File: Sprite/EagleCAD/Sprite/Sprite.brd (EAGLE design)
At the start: 35 x 35 mm, 22 parts, among them Q1 26MHz, U1 CC430F5137, U2 HMC5883LSMD, U3 ITG-3200

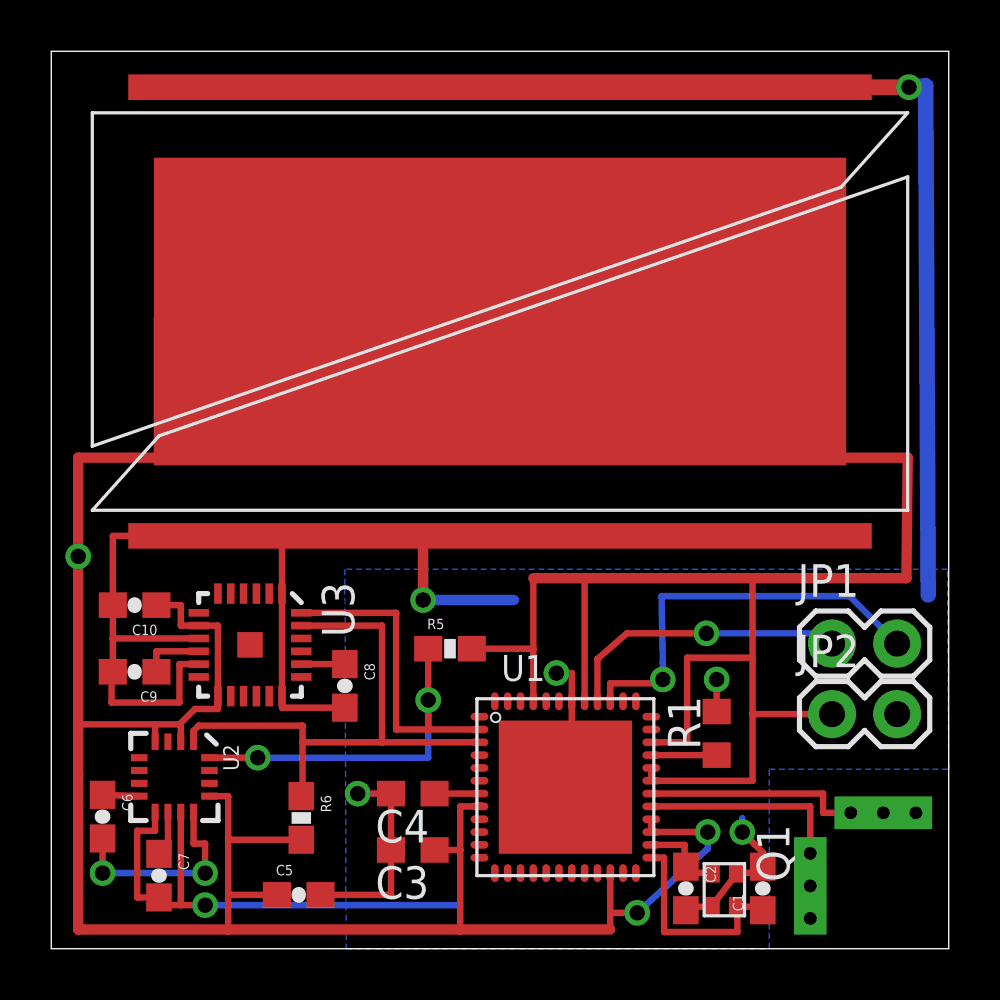
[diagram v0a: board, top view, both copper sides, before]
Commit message: Revert "Moved GND strip closer to TASC cells + removed bottom cells"
This reverts commit a51b0ba4fb3e3dccbe7975012f3db8ac667cb900.
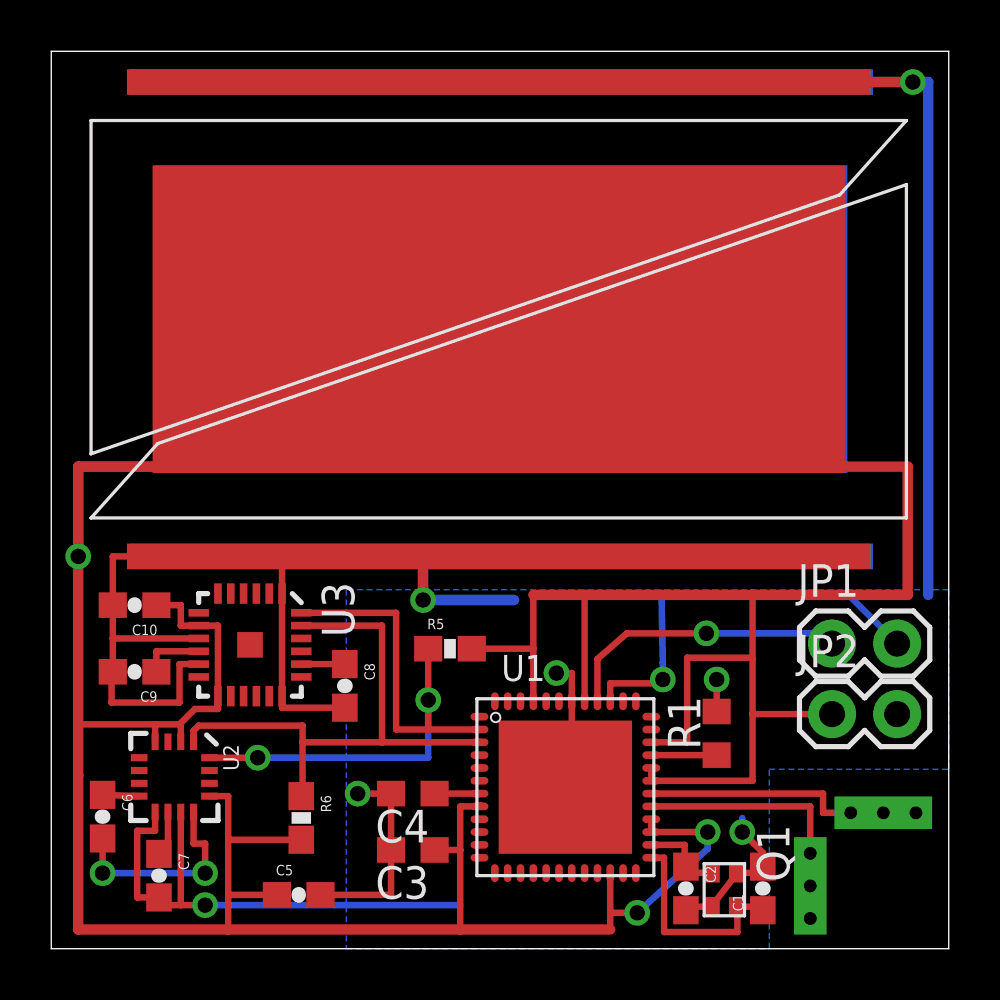
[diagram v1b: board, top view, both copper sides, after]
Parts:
- added S2: TASC, TASC:TASC
- moved S1 0.30 mm to (1.55, 16.8)
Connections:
- net GND: now also S2.MINUS1, S2.MINUS2
- net VCC: now also S2.PLUS
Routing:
- net VCC: track 158.8 -> 182.9 mm
- net GND: track 131.1 -> 137.9 mm
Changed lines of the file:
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@@
 </autorouter>
 <elements>
-<element name="S1" library="TASC" package="TASC" value="TASC" x="1.6" y="17.1"/>
+<element name="S1" library="TASC" package="TASC" value="TASC" x="1.55" y="16.8"/>
+<element name="S2" library="TASC" package="TASC" value="TASC" x="33.45" y="16.8" rot="MR0"/>
 <element name="U1" library="TI_MSP430_v16" package="RGZ48" value="CC430F5137" x="20.05" y="6.3"/>
 <element name="Q1" library="ABM11_JAA" package="ABM11_CERAMIC-SMD-CRYSTAL" value="26MHz" x="26.25" y="2.3" rot="R270"/>
@@
 <signal name="VCC">
 <contactref element="S1" pad="PLUS"/>
+<contactref element="S2" pad="PLUS"/>
 <contactref element="U1" pad="27"/>
 <contactref element="U1" pad="22"/>
@@
 <contactref element="R5" pad="2"/>
 <contactref element="R6" pad="2"/>
-<wire x1="17.5" y1="24.85" x2="4.2" y2="24.55" width="0.4064" layer="1"/>
-<wire x1="4.2" y1="24.55" x2="4.2" y2="19.15" width="0.4064" layer="1"/>
-<wire x1="4.2" y1="19.15" x2="1.05" y2="19.15" width="0.4064" layer="1"/>
-<wire x1="1.05" y1="19.15" x2="1.05" y2="15.3" width="0.4064" layer="1"/>
+<wire x1="17.45" y1="24.55" x2="4.2" y2="24.55" width="0.4064" layer="1"/>
+<wire x1="4.2" y1="24.55" x2="4.2" y2="18.8" width="0.4064" layer="1"/>
+<wire x1="4.2" y1="18.8" x2="1.05" y2="18.8" width="0.4064" layer="1"/>
+<wire x1="1.05" y1="18.8" x2="1.05" y2="15.3" width="0.4064" layer="1"/>
+<wire x1="17.55" y1="24.55" x2="4.2" y2="24.55" width="0.4064" layer="16"/>
+<wire x1="4.2" y1="24.55" x2="4.2" y2="18.8" width="0.4064" layer="16"/>
+<wire x1="4.2" y1="18.8" x2="1.05" y2="18.8" width="0.4064" layer="16"/>
+<wire x1="1.05" y1="18.8" x2="1.05" y2="15.3" width="0.4064" layer="16"/>
 <via x="1.05" y="15.3" extent="1-16" drill="0.6"/>
 <wire x1="16.7" y1="5.55" x2="16.75" y2="5.6" width="0.254" layer="1"/>
-<wire x1="33.35" y1="14.45" x2="33.4" y2="19.15" width="0.4064" layer="1"/>
-<wire x1="33.4" y1="19.15" x2="30.7" y2="19.15" width="0.4064" layer="1"/>
+<wire x1="33.4" y1="13.8" x2="33.4" y2="18.8" width="0.4064" layer="1"/>
+<wire x1="33.4" y1="18.8" x2="30.7" y2="18.8" width="0.4064" layer="1"/>
 <wire x1="16.7" y1="5.55" x2="15.95" y2="5.55" width="0.254" layer="1"/>
 <wire x1="15.95" y1="3.85" x2="14.95" y2="3.85" width="0.254" layer="1"/>
-<wire x1="33.35" y1="14.45" x2="27.35" y2="14.45" width="0.4064" layer="1"/>
-<wire x1="27.35" y1="14.45" x2="20.8" y2="14.45" width="0.4064" layer="1"/>
-<wire x1="20.8" y1="14.45" x2="18.8" y2="14.45" width="0.4064" layer="1"/>
+<wire x1="33.4" y1="13.8" x2="27.35" y2="13.8" width="0.4064" layer="1"/>
+<wire x1="27.35" y1="13.8" x2="20.8" y2="13.8" width="0.4064" layer="1"/>
+<wire x1="20.8" y1="13.8" x2="18.8" y2="13.8" width="0.4064" layer="1"/>
 <wire x1="18.8" y1="9.65" x2="18.8" y2="11.7" width="0.254" layer="1"/>
-<wire x1="18.8" y1="11.7" x2="18.8" y2="14.45" width="0.254" layer="1"/>
+<wire x1="18.8" y1="11.7" x2="18.8" y2="13.8" width="0.254" layer="1"/>
 <wire x1="1.05" y1="15.3" x2="1.05" y2="8.75" width="0.4064" layer="1"/>
 <wire x1="1.05" y1="8.75" x2="1.05" y2="6.75" width="0.4064" layer="1"/>
@@
 <wire x1="27.35" y1="9.15" x2="27.35" y2="11.3" width="0.254" layer="1"/>
 <via x="25.6" y="4.55" extent="1-16" drill="0.6"/>
-<wire x1="27.35" y1="11.3" x2="27.35" y2="14.45" width="0.254" layer="1"/>
+<wire x1="27.35" y1="11.3" x2="27.35" y2="13.8" width="0.254" layer="1"/>
 <wire x1="25.6" y1="4.55" x2="25.6" y2="3.9" width="0.254" layer="16"/>
 <wire x1="25.6" y1="3.9" x2="22.85" y2="1.4" width="0.254" layer="16"/>
@@
 <wire x1="9.75" y1="4.25" x2="6.9" y2="4.25" width="0.254" layer="1"/>
 <wire x1="16.4" y1="11.7" x2="18.8" y2="11.7" width="0.254" layer="1"/>
-<wire x1="20.8" y1="9.65" x2="20.8" y2="14.45" width="0.254" layer="1"/>
+<wire x1="20.8" y1="9.65" x2="20.8" y2="13.8" width="0.254" layer="1"/>
 <wire x1="23.4" y1="8.05" x2="24.8" y2="8.05" width="0.254" layer="1"/>
 <wire x1="24.8" y1="8.05" x2="24.8" y2="11.35" width="0.254" layer="1"/>
@@
 <contactref element="S1" pad="MINUS1"/>
 <contactref element="S1" pad="MINUS2"/>
+<contactref element="S2" pad="MINUS1"/>
+<contactref element="S2" pad="MINUS2"/>
 <contactref element="C4" pad="2"/>
 <contactref element="U1" pad="TP"/>
@@
 <contactref element="U3" pad="1"/>
 <polygon width="0.4064" layer="16">
-<vertex x="11.45" y="14.8"/>
+<vertex x="11.5" y="14"/>
 <vertex x="11.5" y="0"/>
 <vertex x="28" y="0"/>
 <vertex x="28" y="7"/>
 <vertex x="35" y="7"/>
-<vertex x="34.95" y="14.8"/>
+<vertex x="35" y="14"/>
 </polygon>
-<wire x1="17.5" y1="33.6" x2="33.45" y2="33.6" width="0.6096" layer="1"/>
-<via x="33.45" y="33.6" extent="1-16" drill="0.6"/>
-<wire x1="33.45" y1="33.6" x2="34.1" y2="33.65" width="0.6096" layer="16"/>
-<wire x1="34.1" y1="33.65" x2="34.2" y2="13.8" width="0.6096" layer="16"/>
-<wire x1="17.5" y1="16.1" x2="14.6" y2="16.1" width="0.4064" layer="1"/>
+<wire x1="17.45" y1="33.8" x2="33.6" y2="33.8" width="0.4064" layer="1"/>
+<via x="33.6" y="33.8" extent="1-16" drill="0.6"/>
+<wire x1="33.6" y1="33.8" x2="34.2" y2="33.8" width="0.4064" layer="16"/>
+<wire x1="34.2" y1="33.8" x2="34.2" y2="13.8" width="0.4064" layer="16"/>
+<wire x1="17.55" y1="33.8" x2="33.6" y2="33.8" width="0.4064" layer="16"/>
+<wire x1="17.45" y1="15.3" x2="14.5" y2="15.35" width="0.4064" layer="1"/>
 <via x="14.5" y="13.6" extent="1-16" drill="0.6"/>
-<wire x1="14.6" y1="16.1" x2="14.5" y2="16.1" width="0.4064" layer="1"/>
 <wire x1="14.5" y1="13.6" x2="18.05" y2="13.6" width="0.4064" layer="16"/>
-<wire x1="14.5" y1="16.1" x2="14.5" y2="13.6" width="0.4064" layer="1"/>
+<wire x1="14.5" y1="15.35" x2="14.5" y2="13.6" width="0.4064" layer="1"/>
+<wire x1="17.55" y1="15.3" x2="14.5" y2="15.3" width="0.4064" layer="16"/>
 <wire x1="14.5" y1="15.3" x2="14.5" y2="13.6" width="0.4064" layer="16"/>
 <via x="26.95" y="4.55" extent="1-16" drill="0.6"/>
@@
 <wire x1="5.05" y1="5.33" x2="5.05" y2="1.7" width="0.254" layer="1"/>
 <wire x1="5.75" y1="12.1" x2="2.4" y2="12.1" width="0.254" layer="1"/>
-<wire x1="2.4" y1="13.4" x2="2.4" y2="16.1" width="0.254" layer="1"/>
-<wire x1="2.4" y1="16.1" x2="14.6" y2="16.1" width="0.254" layer="1"/>
+<wire x1="2.4" y1="13.4" x2="2.4" y2="15.3" width="0.254" layer="1"/>
+<wire x1="2.4" y1="15.3" x2="4.3" y2="15.3" width="0.254" layer="1"/>
+<wire x1="4.3" y1="15.3" x2="4.3" y2="15.25" width="0.254" layer="1"/>
 <wire x1="2.4" y1="12.1" x2="2.4" y2="10.8" width="0.254" layer="1"/>
 <wire x1="2.4" y1="13.4" x2="2.4" y2="12.1" width="0.254" layer="1"/>
-<wire x1="9" y1="13.85" x2="9" y2="16.05" width="0.254" layer="1"/>
-<wire x1="9" y1="16.05" x2="14.5" y2="16.1" width="0.254" layer="1"/>
+<wire x1="9" y1="13.85" x2="9" y2="15.3" width="0.254" layer="1"/>
+<wire x1="9" y1="15.3" x2="14.5" y2="15.35" width="0.254" layer="1"/>
 <wire x1="9" y1="9.85" x2="9" y2="9.4" width="0.254" layer="1"/>
 <wire x1="9" y1="9.4" x2="11.45" y2="9.4" width="0.254" layer="1"/>
@@
 <wire x1="26.758" y1="2.9604" x2="27.5104" y2="2.9604" width="0.254" layer="1"/>
 <wire x1="27.5104" y1="2.9604" x2="27.75" y2="3.2" width="0.254" layer="1"/>
-<wire x1="2.4" y1="10.8" x2="2.35" y2="10.85" width="0" layer="19" extent="1-1"/>
+<wire x1="2.35" y1="10.85" x2="2.4" y2="10.8" width="0" layer="19" extent="1-1"/>
+<wire x1="9" y1="9.85" x2="5.75" y2="11.1" width="0" layer="19" extent="1-1"/>
 </signal>
 <signal name="N$1">

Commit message: Revert "Revert "Moved GND strip closer to TASC cells + removed bottom cells""
This reverts commit 1dc39e584056e569c73cdb2ce6a50d93971a399e.
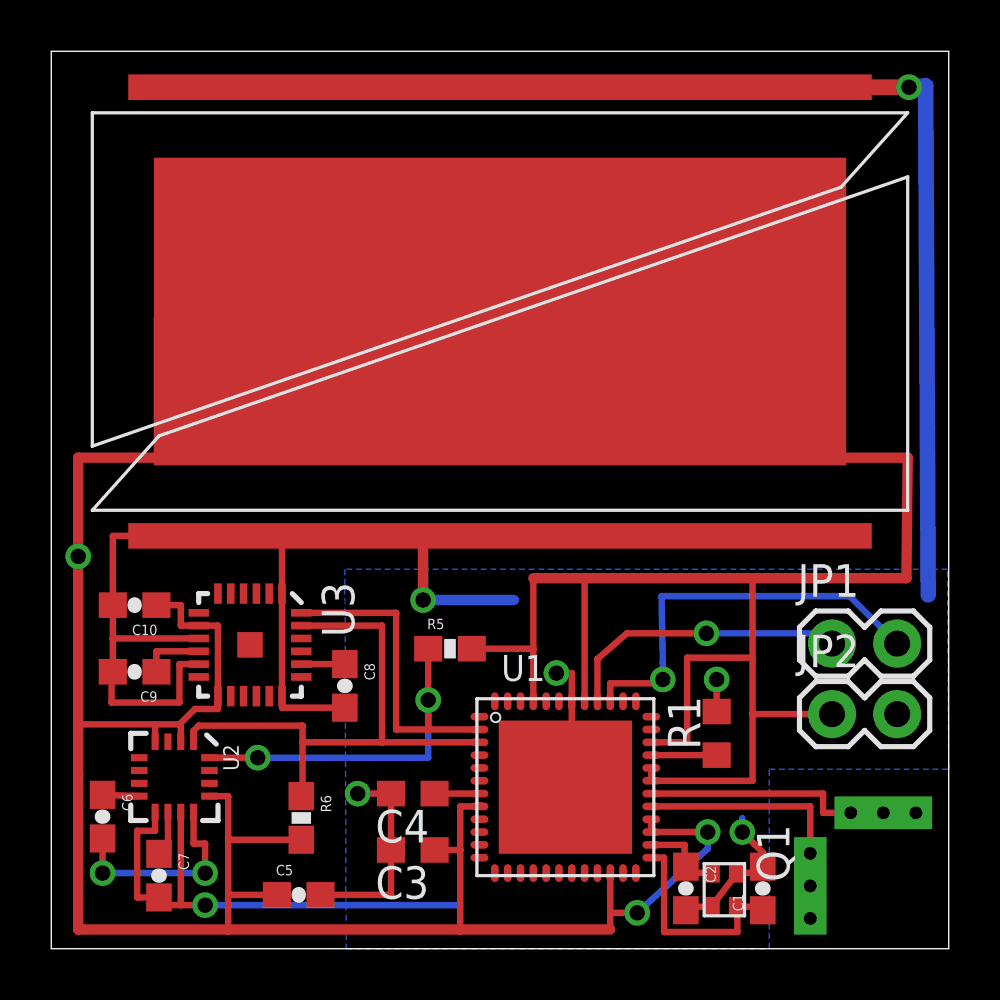
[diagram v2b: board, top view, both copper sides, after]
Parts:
- removed S2: TASC, TASC:TASC
- moved S1 0.30 mm to (1.60, 17.1)
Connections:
- net GND: no longer S2.MINUS1, S2.MINUS2
- net VCC: no longer S2.PLUS
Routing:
- net VCC: track 182.9 -> 158.8 mm
- net GND: track 137.9 -> 131.1 mm
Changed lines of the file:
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@@
 </autorouter>
 <elements>
-<element name="S1" library="TASC" package="TASC" value="TASC" x="1.55" y="16.8"/>
-<element name="S2" library="TASC" package="TASC" value="TASC" x="33.45" y="16.8" rot="MR0"/>
+<element name="S1" library="TASC" package="TASC" value="TASC" x="1.6" y="17.1"/>
 <element name="U1" library="TI_MSP430_v16" package="RGZ48" value="CC430F5137" x="20.05" y="6.3"/>
 <element name="Q1" library="ABM11_JAA" package="ABM11_CERAMIC-SMD-CRYSTAL" value="26MHz" x="26.25" y="2.3" rot="R270"/>
@@
 <signal name="VCC">
 <contactref element="S1" pad="PLUS"/>
-<contactref element="S2" pad="PLUS"/>
 <contactref element="U1" pad="27"/>
 <contactref element="U1" pad="22"/>
@@
 <contactref element="R5" pad="2"/>
 <contactref element="R6" pad="2"/>
-<wire x1="17.45" y1="24.55" x2="4.2" y2="24.55" width="0.4064" layer="1"/>
-<wire x1="4.2" y1="24.55" x2="4.2" y2="18.8" width="0.4064" layer="1"/>
-<wire x1="4.2" y1="18.8" x2="1.05" y2="18.8" width="0.4064" layer="1"/>
-<wire x1="1.05" y1="18.8" x2="1.05" y2="15.3" width="0.4064" layer="1"/>
-<wire x1="17.55" y1="24.55" x2="4.2" y2="24.55" width="0.4064" layer="16"/>
-<wire x1="4.2" y1="24.55" x2="4.2" y2="18.8" width="0.4064" layer="16"/>
-<wire x1="4.2" y1="18.8" x2="1.05" y2="18.8" width="0.4064" layer="16"/>
-<wire x1="1.05" y1="18.8" x2="1.05" y2="15.3" width="0.4064" layer="16"/>
+<wire x1="17.5" y1="24.85" x2="4.2" y2="24.55" width="0.4064" layer="1"/>
+<wire x1="4.2" y1="24.55" x2="4.2" y2="19.15" width="0.4064" layer="1"/>
+<wire x1="4.2" y1="19.15" x2="1.05" y2="19.15" width="0.4064" layer="1"/>
+<wire x1="1.05" y1="19.15" x2="1.05" y2="15.3" width="0.4064" layer="1"/>
 <via x="1.05" y="15.3" extent="1-16" drill="0.6"/>
 <wire x1="16.7" y1="5.55" x2="16.75" y2="5.6" width="0.254" layer="1"/>
-<wire x1="33.4" y1="13.8" x2="33.4" y2="18.8" width="0.4064" layer="1"/>
-<wire x1="33.4" y1="18.8" x2="30.7" y2="18.8" width="0.4064" layer="1"/>
+<wire x1="33.35" y1="14.45" x2="33.4" y2="19.15" width="0.4064" layer="1"/>
+<wire x1="33.4" y1="19.15" x2="30.7" y2="19.15" width="0.4064" layer="1"/>
 <wire x1="16.7" y1="5.55" x2="15.95" y2="5.55" width="0.254" layer="1"/>
 <wire x1="15.95" y1="3.85" x2="14.95" y2="3.85" width="0.254" layer="1"/>
-<wire x1="33.4" y1="13.8" x2="27.35" y2="13.8" width="0.4064" layer="1"/>
-<wire x1="27.35" y1="13.8" x2="20.8" y2="13.8" width="0.4064" layer="1"/>
-<wire x1="20.8" y1="13.8" x2="18.8" y2="13.8" width="0.4064" layer="1"/>
+<wire x1="33.35" y1="14.45" x2="27.35" y2="14.45" width="0.4064" layer="1"/>
+<wire x1="27.35" y1="14.45" x2="20.8" y2="14.45" width="0.4064" layer="1"/>
+<wire x1="20.8" y1="14.45" x2="18.8" y2="14.45" width="0.4064" layer="1"/>
 <wire x1="18.8" y1="9.65" x2="18.8" y2="11.7" width="0.254" layer="1"/>
-<wire x1="18.8" y1="11.7" x2="18.8" y2="13.8" width="0.254" layer="1"/>
+<wire x1="18.8" y1="11.7" x2="18.8" y2="14.45" width="0.254" layer="1"/>
 <wire x1="1.05" y1="15.3" x2="1.05" y2="8.75" width="0.4064" layer="1"/>
 <wire x1="1.05" y1="8.75" x2="1.05" y2="6.75" width="0.4064" layer="1"/>
@@
 <wire x1="27.35" y1="9.15" x2="27.35" y2="11.3" width="0.254" layer="1"/>
 <via x="25.6" y="4.55" extent="1-16" drill="0.6"/>
-<wire x1="27.35" y1="11.3" x2="27.35" y2="13.8" width="0.254" layer="1"/>
+<wire x1="27.35" y1="11.3" x2="27.35" y2="14.45" width="0.254" layer="1"/>
 <wire x1="25.6" y1="4.55" x2="25.6" y2="3.9" width="0.254" layer="16"/>
 <wire x1="25.6" y1="3.9" x2="22.85" y2="1.4" width="0.254" layer="16"/>
@@
 <wire x1="9.75" y1="4.25" x2="6.9" y2="4.25" width="0.254" layer="1"/>
 <wire x1="16.4" y1="11.7" x2="18.8" y2="11.7" width="0.254" layer="1"/>
-<wire x1="20.8" y1="9.65" x2="20.8" y2="13.8" width="0.254" layer="1"/>
+<wire x1="20.8" y1="9.65" x2="20.8" y2="14.45" width="0.254" layer="1"/>
 <wire x1="23.4" y1="8.05" x2="24.8" y2="8.05" width="0.254" layer="1"/>
 <wire x1="24.8" y1="8.05" x2="24.8" y2="11.35" width="0.254" layer="1"/>
@@
 <contactref element="S1" pad="MINUS1"/>
 <contactref element="S1" pad="MINUS2"/>
-<contactref element="S2" pad="MINUS1"/>
-<contactref element="S2" pad="MINUS2"/>
 <contactref element="C4" pad="2"/>
 <contactref element="U1" pad="TP"/>
@@
 <contactref element="U3" pad="1"/>
 <polygon width="0.4064" layer="16">
-<vertex x="11.5" y="14"/>
+<vertex x="11.45" y="14.8"/>
 <vertex x="11.5" y="0"/>
 <vertex x="28" y="0"/>
 <vertex x="28" y="7"/>
 <vertex x="35" y="7"/>
-<vertex x="35" y="14"/>
+<vertex x="34.95" y="14.8"/>
 </polygon>
-<wire x1="17.45" y1="33.8" x2="33.6" y2="33.8" width="0.4064" layer="1"/>
-<via x="33.6" y="33.8" extent="1-16" drill="0.6"/>
-<wire x1="33.6" y1="33.8" x2="34.2" y2="33.8" width="0.4064" layer="16"/>
-<wire x1="34.2" y1="33.8" x2="34.2" y2="13.8" width="0.4064" layer="16"/>
-<wire x1="17.55" y1="33.8" x2="33.6" y2="33.8" width="0.4064" layer="16"/>
-<wire x1="17.45" y1="15.3" x2="14.5" y2="15.35" width="0.4064" layer="1"/>
+<wire x1="17.5" y1="33.6" x2="33.45" y2="33.6" width="0.6096" layer="1"/>
+<via x="33.45" y="33.6" extent="1-16" drill="0.6"/>
+<wire x1="33.45" y1="33.6" x2="34.1" y2="33.65" width="0.6096" layer="16"/>
+<wire x1="34.1" y1="33.65" x2="34.2" y2="13.8" width="0.6096" layer="16"/>
+<wire x1="17.5" y1="16.1" x2="14.6" y2="16.1" width="0.4064" layer="1"/>
 <via x="14.5" y="13.6" extent="1-16" drill="0.6"/>
+<wire x1="14.6" y1="16.1" x2="14.5" y2="16.1" width="0.4064" layer="1"/>
 <wire x1="14.5" y1="13.6" x2="18.05" y2="13.6" width="0.4064" layer="16"/>
-<wire x1="14.5" y1="15.35" x2="14.5" y2="13.6" width="0.4064" layer="1"/>
-<wire x1="17.55" y1="15.3" x2="14.5" y2="15.3" width="0.4064" layer="16"/>
+<wire x1="14.5" y1="16.1" x2="14.5" y2="13.6" width="0.4064" layer="1"/>
 <wire x1="14.5" y1="15.3" x2="14.5" y2="13.6" width="0.4064" layer="16"/>
 <via x="26.95" y="4.55" extent="1-16" drill="0.6"/>
@@
 <wire x1="5.05" y1="5.33" x2="5.05" y2="1.7" width="0.254" layer="1"/>
 <wire x1="5.75" y1="12.1" x2="2.4" y2="12.1" width="0.254" layer="1"/>
-<wire x1="2.4" y1="13.4" x2="2.4" y2="15.3" width="0.254" layer="1"/>
-<wire x1="2.4" y1="15.3" x2="4.3" y2="15.3" width="0.254" layer="1"/>
-<wire x1="4.3" y1="15.3" x2="4.3" y2="15.25" width="0.254" layer="1"/>
+<wire x1="2.4" y1="13.4" x2="2.4" y2="16.1" width="0.254" layer="1"/>
+<wire x1="2.4" y1="16.1" x2="14.6" y2="16.1" width="0.254" layer="1"/>
 <wire x1="2.4" y1="12.1" x2="2.4" y2="10.8" width="0.254" layer="1"/>
 <wire x1="2.4" y1="13.4" x2="2.4" y2="12.1" width="0.254" layer="1"/>
-<wire x1="9" y1="13.85" x2="9" y2="15.3" width="0.254" layer="1"/>
-<wire x1="9" y1="15.3" x2="14.5" y2="15.35" width="0.254" layer="1"/>
+<wire x1="9" y1="13.85" x2="9" y2="16.05" width="0.254" layer="1"/>
+<wire x1="9" y1="16.05" x2="14.5" y2="16.1" width="0.254" layer="1"/>
 <wire x1="9" y1="9.85" x2="9" y2="9.4" width="0.254" layer="1"/>
 <wire x1="9" y1="9.4" x2="11.45" y2="9.4" width="0.254" layer="1"/>
@@
 <wire x1="26.758" y1="2.9604" x2="27.5104" y2="2.9604" width="0.254" layer="1"/>
 <wire x1="27.5104" y1="2.9604" x2="27.75" y2="3.2" width="0.254" layer="1"/>
-<wire x1="2.35" y1="10.85" x2="2.4" y2="10.8" width="0" layer="19" extent="1-1"/>
-<wire x1="9" y1="9.85" x2="5.75" y2="11.1" width="0" layer="19" extent="1-1"/>
+<wire x1="2.4" y1="10.8" x2="2.35" y2="10.85" width="0" layer="19" extent="1-1"/>
 </signal>
 <signal name="N$1">
